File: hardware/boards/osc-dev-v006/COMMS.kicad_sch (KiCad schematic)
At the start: 9 parts, among them J5 JST-ZH-H, J6 PIN-1-2P, J7 PIN-1-5P, J8 PIN-2-2P

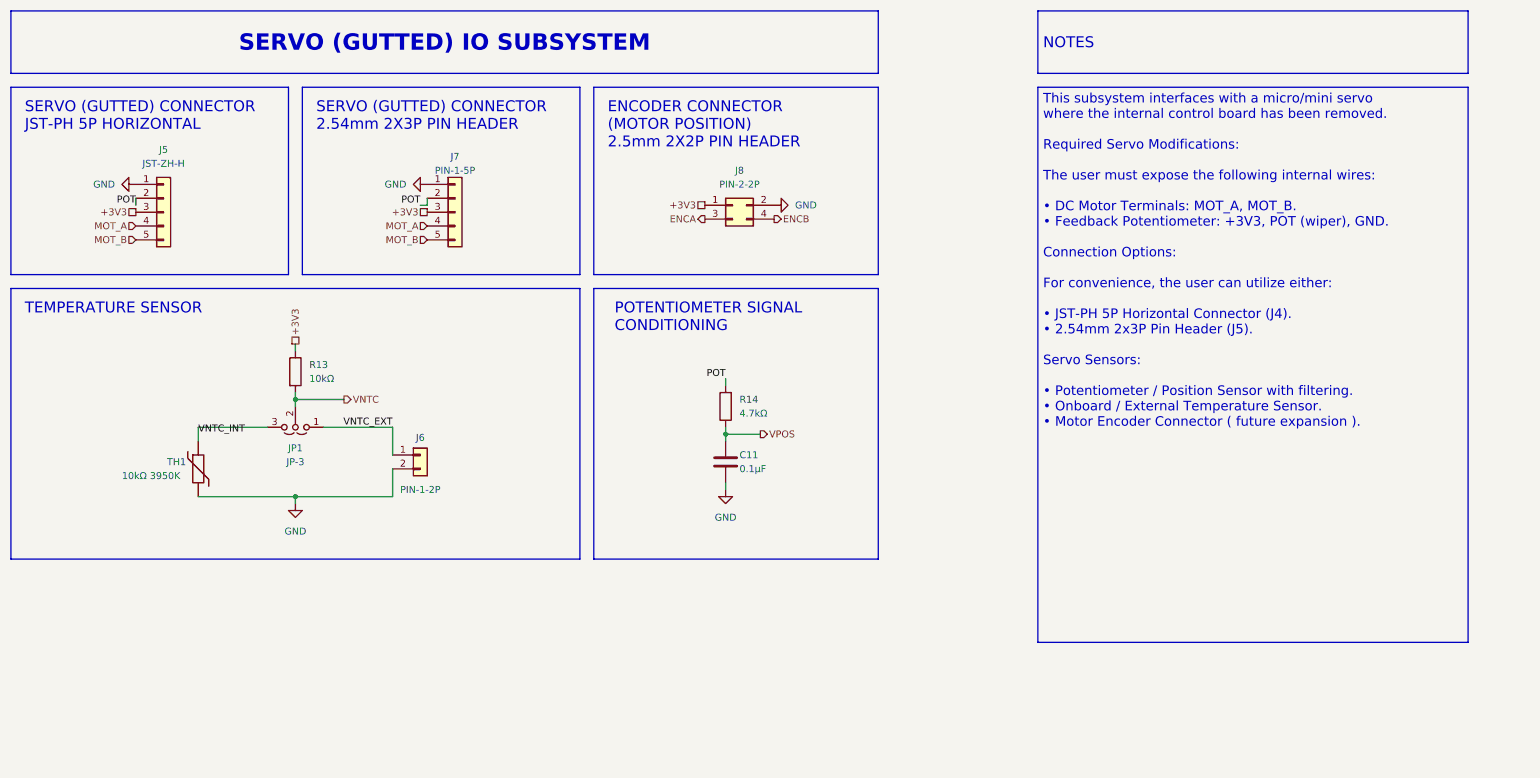
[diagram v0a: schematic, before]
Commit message: rename board to osc-dev-v006
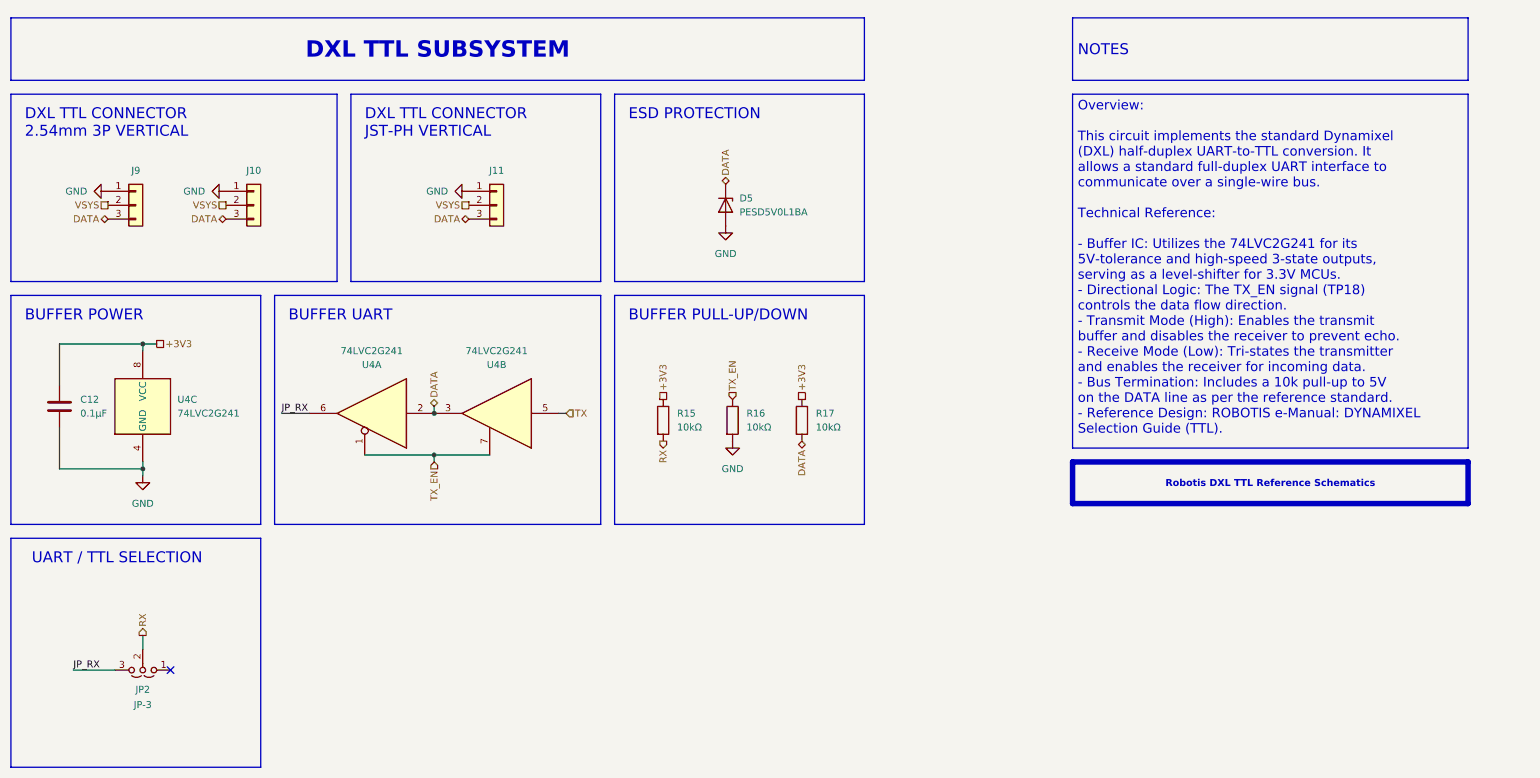
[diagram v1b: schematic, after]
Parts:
- removed C11: 0.1µF, Capacitor_SMD:C_0805_2012Metric_Pad1.18x1.45mm_HandSolder, symbol Device:C
- removed J5: JST-ZH-H, shared:CONN-TH_S5B-ZR-LF-SN, symbol Connector_Generic:Conn_01x05
- removed J6: PIN-1-2P, Connector_PinHeader_2.54mm:PinHeader_1x02_P2.54mm_Vertical, symbol Connector_Generic:Conn_01x02
- removed J7: PIN-1-5P, Connector_PinHeader_2.54mm:PinHeader_1x05_P2.54mm_Vertical, symbol Connector_Generic:Conn_01x05
- removed J8: PIN-2-2P, Connector_PinHeader_2.54mm:PinHeader_2x02_P2.54mm_Vertical, symbol Connector_Generic:Conn_02x02_Odd_Even
- removed JP1: JP-3, Connector_PinHeader_2.54mm:PinHeader_1x03_P2.54mm_Vertical, symbol Jumper:Jumper_3_Open
- removed R13: 10kΩ, Resistor_SMD:R_0805_2012Metric_Pad1.20x1.40mm_HandSolder, symbol Device:R
- removed R14: 4.7kΩ, Resistor_SMD:R_0805_2012Metric_Pad1.20x1.40mm_HandSolder, symbol Device:R
- removed TH1: 10kΩ 3950K, Resistor_SMD:R_0805_2012Metric_Pad1.20x1.40mm_HandSolder, symbol Device:Thermistor
- added C12: 0.1µF, Capacitor_SMD:C_0805_2012Metric_Pad1.18x1.45mm_HandSolder, symbol Device:C
- added D5: PESD5V0L1BA, Diode_SMD:D_SOD-323_HandSoldering, symbol Diode:PESD5V0L1UL
- added J10, J9: PIN-1-3P, Connector_PinHeader_2.54mm:PinHeader_1x03_P2.54mm_Vertical, symbol Connector_Generic:Conn_01x03
- added J11: JST-PH-V, shared:CONN-TH_B3B-PH-K-S, symbol Connector_Generic:Conn_01x03
- added JP2: JP-3, Connector_PinHeader_2.54mm:PinHeader_1x03_P2.54mm_Vertical, symbol Jumper:Jumper_3_Open
- added R15, R16, R17: 10kΩ, Resistor_SMD:R_0805_2012Metric_Pad1.20x1.40mm_HandSolder, symbol Device:R
- added U4: 74LVC2G241, shared:VSSOP-8_L2.3-W2.0-P0.50-LS3.1-BR, symbol 74xGxx:74LVC2G241
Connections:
- net +3V3: now also C12.1, R15.1, R17.1, U4.8 (VCC)
- net GND: now also C12.2, D5.2 (A), J10.1 (Pin_1), J11.1 (Pin_1), J9.1 (Pin_1), R16.2, U4.4 (GND)
- new net DATA: D5.1 (K), J10.3 (Pin_3), J11.3 (Pin_3), J9.3 (Pin_3), R17.2, U4.2, U4.3
- new net JP_RX: JP2.3 (B), U4.6
- new net RX: JP2.2 (C), R15.2
- new net TX: U4.5
- new net TX_EN: R16.1, U4.1, U4.7
- new net VSYS: J10.2 (Pin_2), J11.2 (Pin_2), J9.2 (Pin_2)
- no-connect marks 0 -> 1
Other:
- note added: "BUFFER POWER"
- note added: "BUFFER PULL-UP/DOWN"
- note added: "BUFFER UART"
- note added: "DXL TTL CONNECTOR 2.54mm 3P VERTICAL"
- note added: "DXL TTL CONNECTOR JST-PH VERTICAL"
- note added: "ESD PROTECTION"
- note added: "UART / TTL SELECTION"
- note removed: "ENCODER CONNECTOR (MOTOR POSITION) 2.5mm 2X2P PIN HEADER"
- note removed: "POTENTIOMETER SIGNAL CONDITIONING"
- note removed: "SERVO (GUTTED) CONNECTOR 2.54mm 2X3P PIN HEADER"
- note removed: "SERVO (GUTTED) CONNECTOR JST-PH 5P HORIZONTAL"
- note removed: "TEMPERATURE SENSOR"
